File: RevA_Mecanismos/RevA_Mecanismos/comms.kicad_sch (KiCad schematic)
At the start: 10 parts, among them IC1 MAX33040EAKA+T, J2 Conn_01x03_Pin, J3 430450224, J4 430450224

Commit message: Created PCB project
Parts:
- added J6, J7: 430450224, MolexConnectors:CON_430450224_MOL, symbol MolexConnectors:430450224
- IC1: footprint footprints:SOT65P280X145-8N -> MAX33040EAKA+T:SOT65P280X145-8N
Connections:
- net GND: now also J6.P1, J6.P2, J7.P1, J7.P2
- new net SCL: J6.1
- new net SDA: J6.2
- new net UART_RX: J7.2
- new net UART_TX: J7.1
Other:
- note added: "Comms"
- note added: "I2C CONNECTOR"
- note added: "UART CONNECTOR"

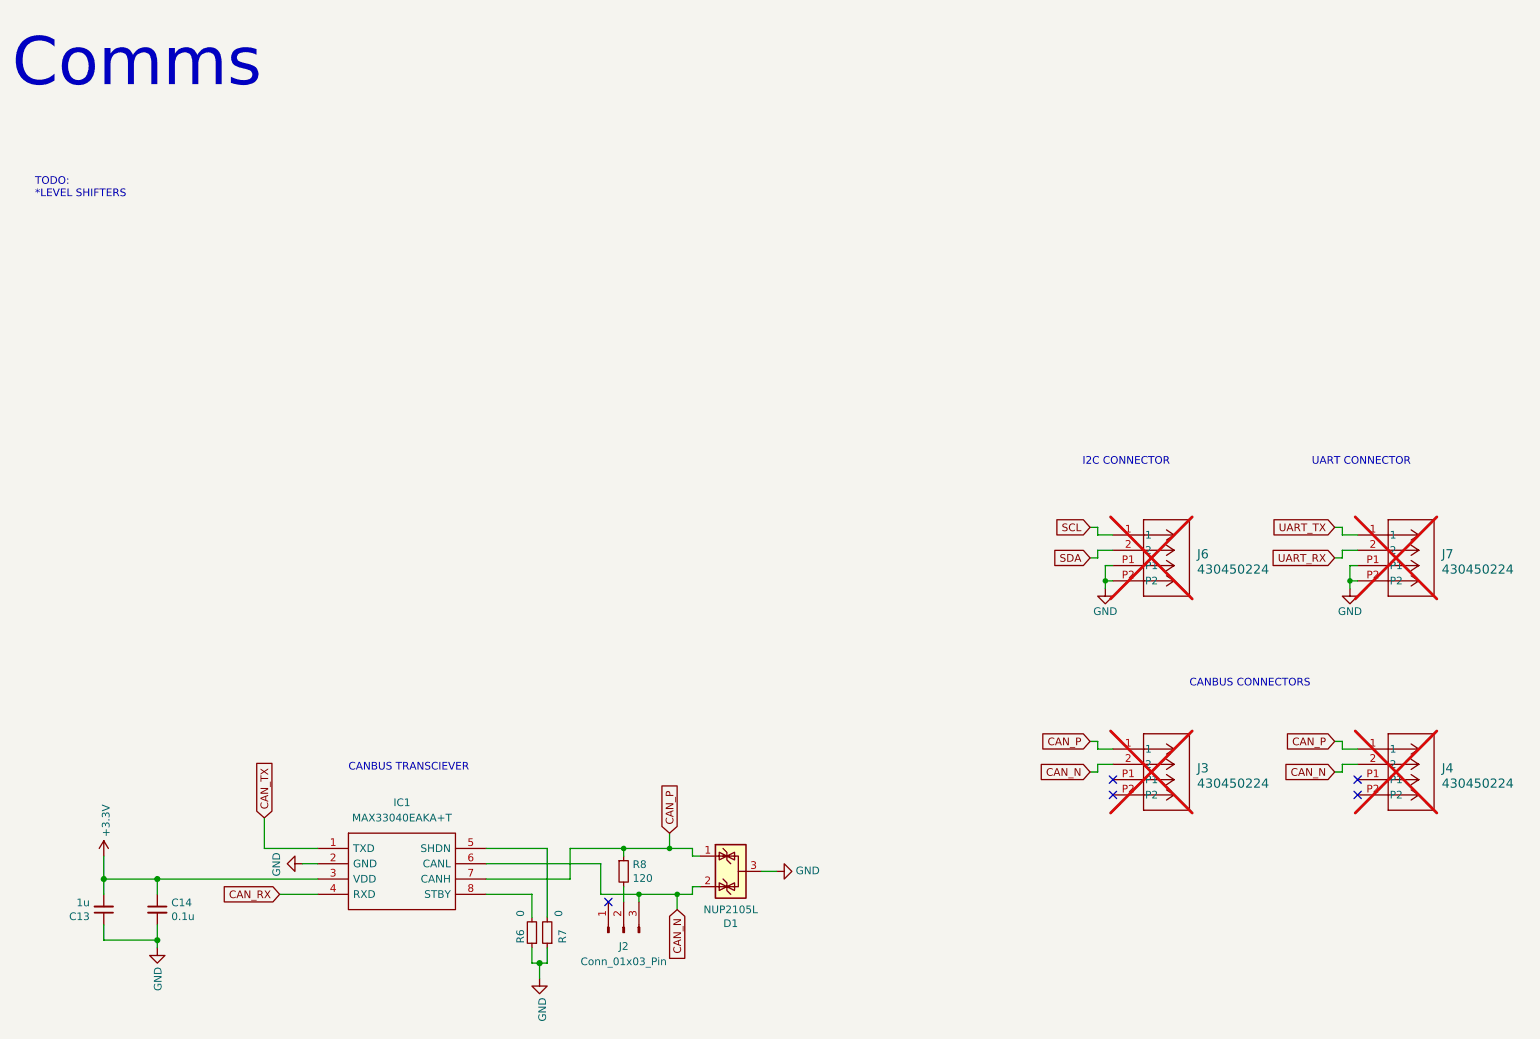
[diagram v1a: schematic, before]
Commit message: Adiciones a secciones de motores y power supply para placa de mecanismos
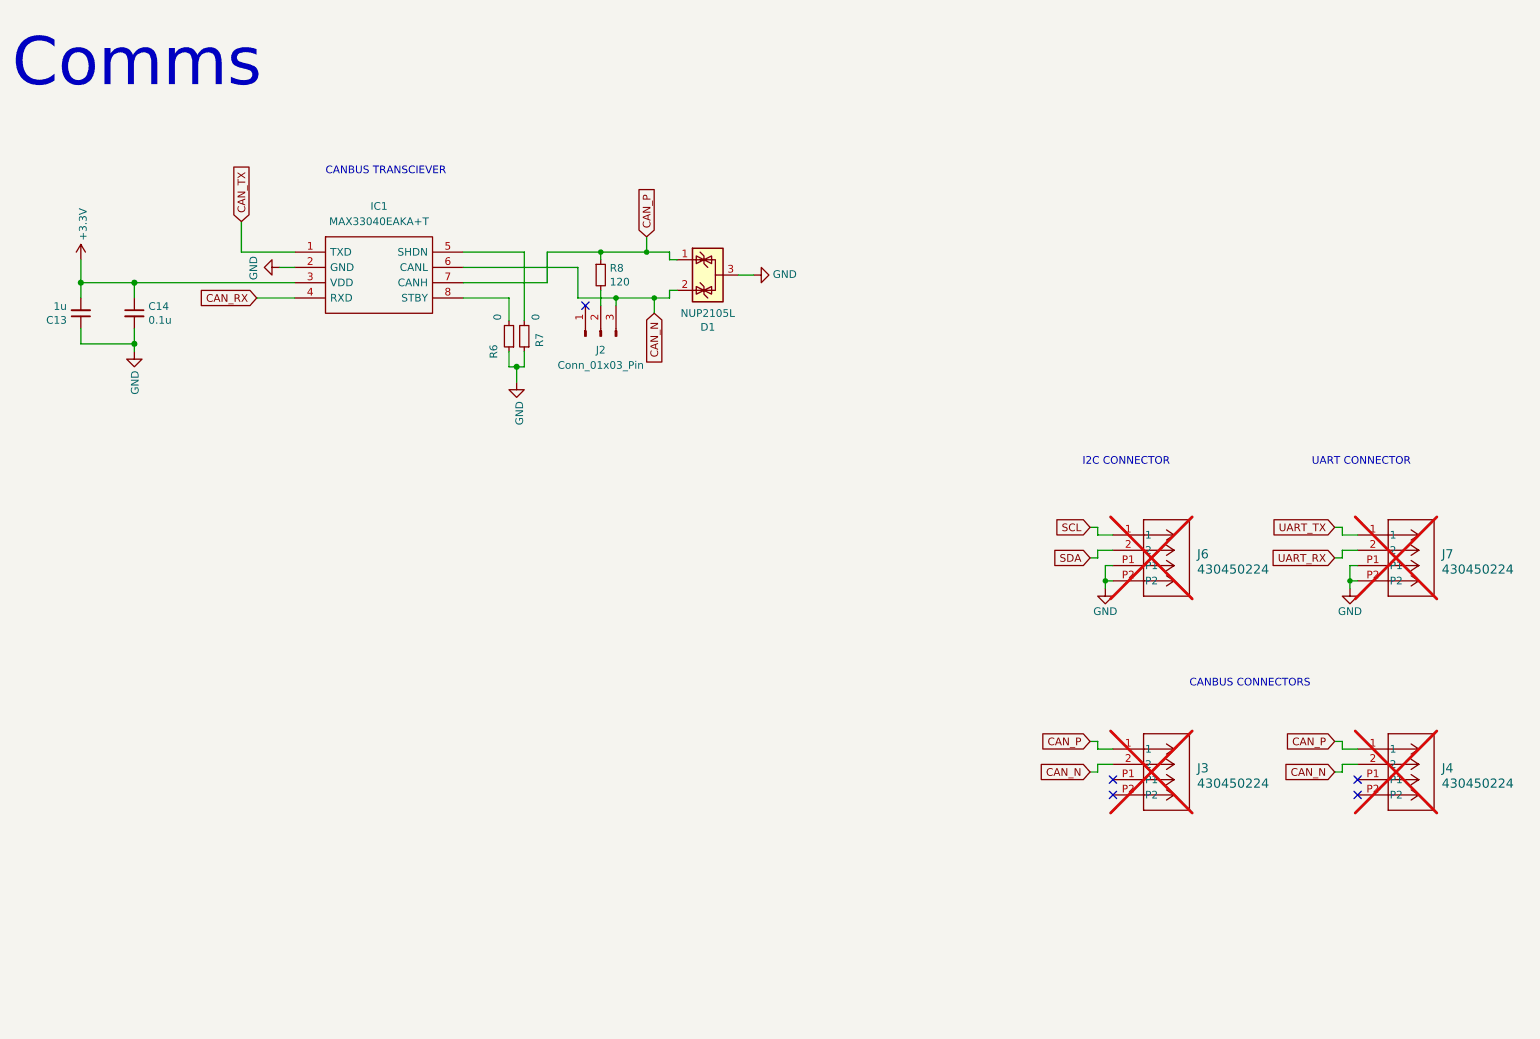
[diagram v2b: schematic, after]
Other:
- note removed: "TODO: *LEVEL SHIFTERS"
- moved on the sheet: C13, C14, D1, IC1, J2, R6, R7, R8

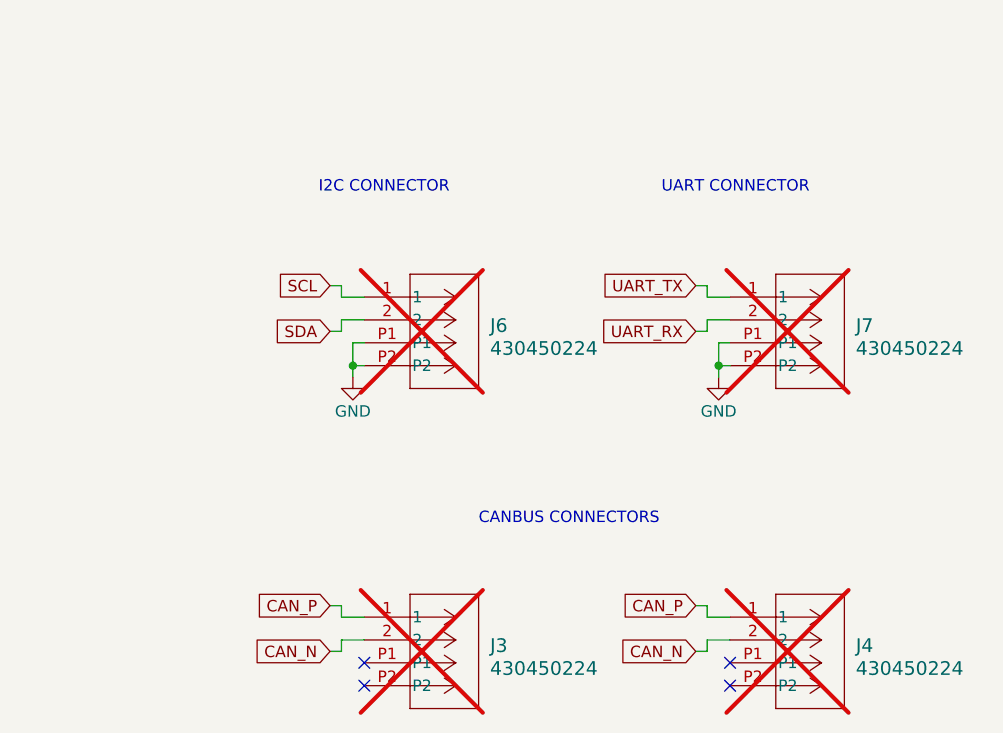
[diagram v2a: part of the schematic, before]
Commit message: Debug connectors and pwr flag to +12v
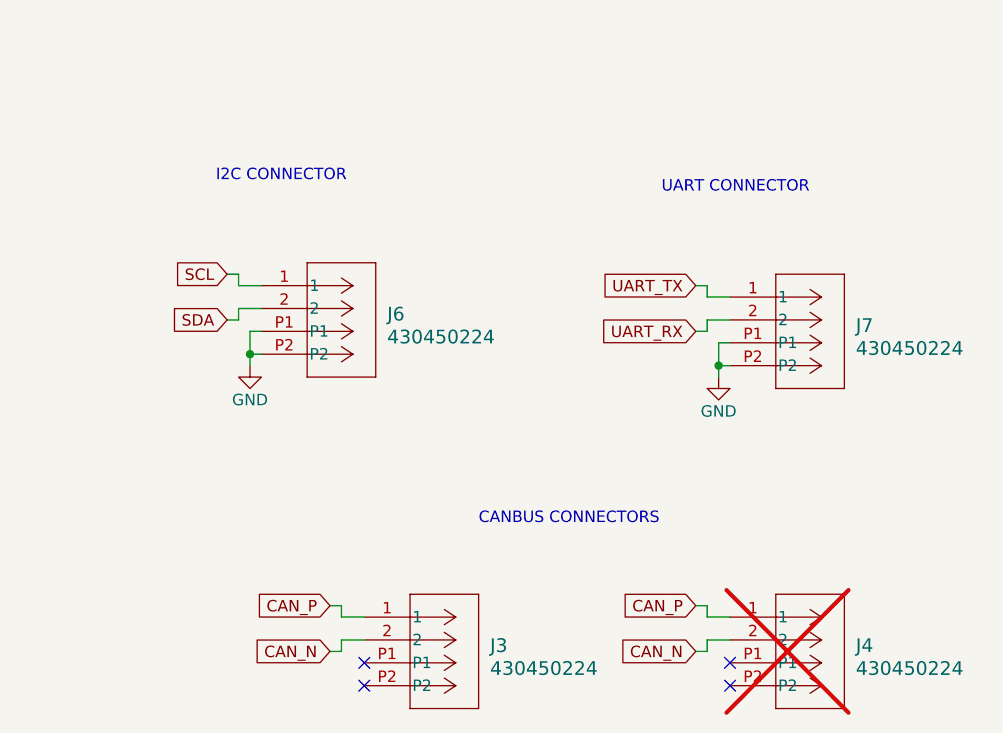
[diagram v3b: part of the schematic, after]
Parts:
- J3, J6, J7: now fitted
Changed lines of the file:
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@@
   (junction (at 106.68 78.74) (diameter 1.016) (color 0 0 0 0)
   )
-  (junction (at 204.47 114.3) (diameter 0) (color 0 0 0 0)
+  (junction (at 193.04 113.03) (diameter 0) (color 0 0 0 0)
   )
   (junction (at 129.54 67.31) (diameter 0) (color 0 0 0 0)
@@
     (stroke (width 0) (type solid))
   )
-  (wire (pts (xy 203.2 110.49) (xy 201.93 110.49))
+  (wire (pts (xy 191.77 109.22) (xy 190.5 109.22))
     (stroke (width 0) (type default))
   )
@@
     (stroke (width 0) (type solid))
   )
-  (wire (pts (xy 203.2 106.68) (xy 205.74 106.68))
-    (stroke (width 0) (type default))
-  )
-  (wire (pts (xy 204.47 115.57) (xy 204.47 114.3))
+  (wire (pts (xy 191.77 105.41) (xy 194.31 105.41))
+    (stroke (width 0) (type default))
+  )
+  (wire (pts (xy 193.04 114.3) (xy 193.04 113.03))
     (stroke (width 0) (type default))
   )
@@
     (stroke (width 0) (type default))
   )
-  (wire (pts (xy 203.2 110.49) (xy 203.2 109.22))
+  (wire (pts (xy 191.77 109.22) (xy 191.77 107.95))
     (stroke (width 0) (type default))
   )
@@
     (stroke (width 0) (type default))
   )
-  (wire (pts (xy 203.2 105.41) (xy 203.2 106.68))
+  (wire (pts (xy 191.77 104.14) (xy 191.77 105.41))
     (stroke (width 0) (type default))
   )
@@
     (stroke (width 0) (type solid))
   )
-  (wire (pts (xy 204.47 111.76) (xy 205.74 111.76))
-    (stroke (width 0) (type default))
-  )
-  (wire (pts (xy 204.47 114.3) (xy 204.47 111.76))
+  (wire (pts (xy 193.04 110.49) (xy 194.31 110.49))
+    (stroke (width 0) (type default))
+  )
+  (wire (pts (xy 193.04 113.03) (xy 193.04 110.49))
     (stroke (width 0) (type default))
   )
@@
     (stroke (width 0) (type default))
   )
-  (wire (pts (xy 203.2 109.22) (xy 205.74 109.22))
+  (wire (pts (xy 191.77 107.95) (xy 194.31 107.95))
     (stroke (width 0) (type default))
   )
@@
     (stroke (width 0) (type solid))
   )
-  (wire (pts (xy 201.93 105.41) (xy 203.2 105.41))
+  (wire (pts (xy 190.5 104.14) (xy 191.77 104.14))
     (stroke (width 0) (type default))
   )
@@
     (stroke (width 0) (type default))
   )
-  (wire (pts (xy 204.47 114.3) (xy 205.74 114.3))
+  (wire (pts (xy 193.04 113.03) (xy 194.31 113.03))
     (stroke (width 0) (type default))
   )
@@
     (effects (font (size 1.27 1.27)) (justify left bottom))
   )
-  (text "I2C CONNECTOR" (at 200.66 95.25 0)
+  (text "I2C CONNECTOR" (at 189.23 93.98 0)
     (effects (font (size 1.27 1.27)) (justify left bottom))
   )
@@
     )
   )
-  (global_label "SCL" (shape input) (at 201.93 105.41 180) (fields_autoplaced)
+  (global_label "SCL" (shape input) (at 190.5 104.14 180) (fields_autoplaced)
     (effects (font (size 1.27 1.27)) (justify right))
-    (property "Intersheetrefs" "${INTERSHEET_REFS}" (at 195.5166 105.41 0)
+    (property "Intersheetrefs" "${INTERSHEET_REFS}" (at 184.0866 104.14 0)
       (effects (font (size 1.27 1.27)) (justify right) hide)
     )
@@
     )
   )
-  (global_label "SDA" (shape input) (at 201.93 110.49 180) (fields_autoplaced)
+  (global_label "SDA" (shape input) (at 190.5 109.22 180) (fields_autoplaced)
     (effects (font (size 1.27 1.27)) (justify right))
-    (property "Intersheetrefs" "${INTERSHEET_REFS}" (at 195.4561 110.49 0)
+    (property "Intersheetrefs" "${INTERSHEET_REFS}" (at 184.0261 109.22 0)
       (effects (font (size 1.27 1.27)) (justify right) hide)
     )
@@
     )
   )
-  (symbol (lib_id "power:GND") (at 204.47 115.57 0) (unit 1)
+  (symbol (lib_id "power:GND") (at 193.04 114.3 0) (unit 1)
     (in_bom yes) (on_board yes) (dnp no)
-    (property "Reference" "#PWR067" (at 204.47 121.92 0)
-      (effects (font (size 1.27 1.27)) hide)
-    )
-    (property "Value" "GND" (at 204.47 119.38 0)
+    (property "Reference" "#PWR067" (at 193.04 120.65 0)
+      (effects (font (size 1.27 1.27)) hide)
+    )
+    (property "Value" "GND" (at 193.04 118.11 0)
       (effects (font (size 1.27 1.27)))
     )
-    (property "Footprint" "" (at 204.47 115.57 0)
-      (effects (font (size 1.27 1.27)) hide)
-    )
-    (property "Datasheet" "" (at 204.47 115.57 0)
+    (property "Footprint" "" (at 193.04 114.3 0)
+      (effects (font (size 1.27 1.27)) hide)
+    )
+    (property "Datasheet" "" (at 193.04 114.3 0)
       (effects (font (size 1.27 1.27)) hide)
     )
@@
   )
   (symbol (lib_id "MolexConnectors:430450224") (at 246.38 106.68 0) (unit 1)
-    (in_bom yes) (on_board yes) (dnp yes) (fields_autoplaced)
+    (in_bom yes) (on_board yes) (dnp no) (fields_autoplaced)
     (property "Reference" "J7" (at 260.35 109.855 0)
       (effects (font (size 1.524 1.524)) (justify left))
@@
     )
   )
-  (symbol (lib_id "MolexConnectors:430450224") (at 205.74 106.68 0) (unit 1)
-    (in_bom yes) (on_board yes) (dnp yes) (fields_autoplaced)
-    (property "Reference" "J6" (at 219.71 109.855 0)
+  (symbol (lib_id "MolexConnectors:430450224") (at 194.31 105.41 0) (unit 1)
+    (in_bom yes) (on_board yes) (dnp no) (fields_autoplaced)
+    (property "Reference" "J6" (at 208.28 108.585 0)
       (effects (font (size 1.524 1.524)) (justify left))
     )
-    (property "Value" "430450224" (at 219.71 112.395 0)
+    (property "Value" "430450224" (at 208.28 111.125 0)
       (effects (font (size 1.524 1.524)) (justify left))
     )
-    (property "Footprint" "MolexConnectors:CON_430450224_MOL" (at 205.74 106.68 0)
+    (property "Footprint" "MolexConnectors:CON_430450224_MOL" (at 194.31 105.41 0)
       (effects (font (size 1.27 1.27) italic) hide)
     )
-    (property "Datasheet" "430450224" (at 205.74 106.68 0)
+    (property "Datasheet" "430450224" (at 194.31 105.41 0)
       (effects (font (size 1.27 1.27) italic) hide)
     )
@@
   )
   (symbol (lib_id "MolexConnectors:430450224") (at 205.74 142.24 0) (unit 1)
-    (in_bom yes) (on_board yes) (dnp yes) (fields_autoplaced)
+    (in_bom yes) (on_board yes) (dnp no) (fields_autoplaced)
     (property "Reference" "J3" (at 219.71 145.415 0)
       (effects (font (size 1.524 1.524)) (justify left))
